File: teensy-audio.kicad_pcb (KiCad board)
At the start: 2 copper layers, 80 x 140 mm, 47 parts, among them J1 AudioJack2, J10 Conn_01x05, J11 Conn_01x02, J2 AudioJack2, J3 Barrel_Jack, J4 Conn_02x08_Odd_Even, J5 Conn_02x08_Odd_Even, J6 Conn_02x05_Odd_Even, J7 Conn_01x04, J8 Conn_01x04, J9 Conn_02x05_Odd_Even, SW1 RotaryEncoder_Switch, SW2/3 SW_Push, SW3/4 SW_Push, SW4/5 SW_Push, SW5/9 SW_Push, U1 LM358, U2 LM7805_TO220, U3 Teensy4.0

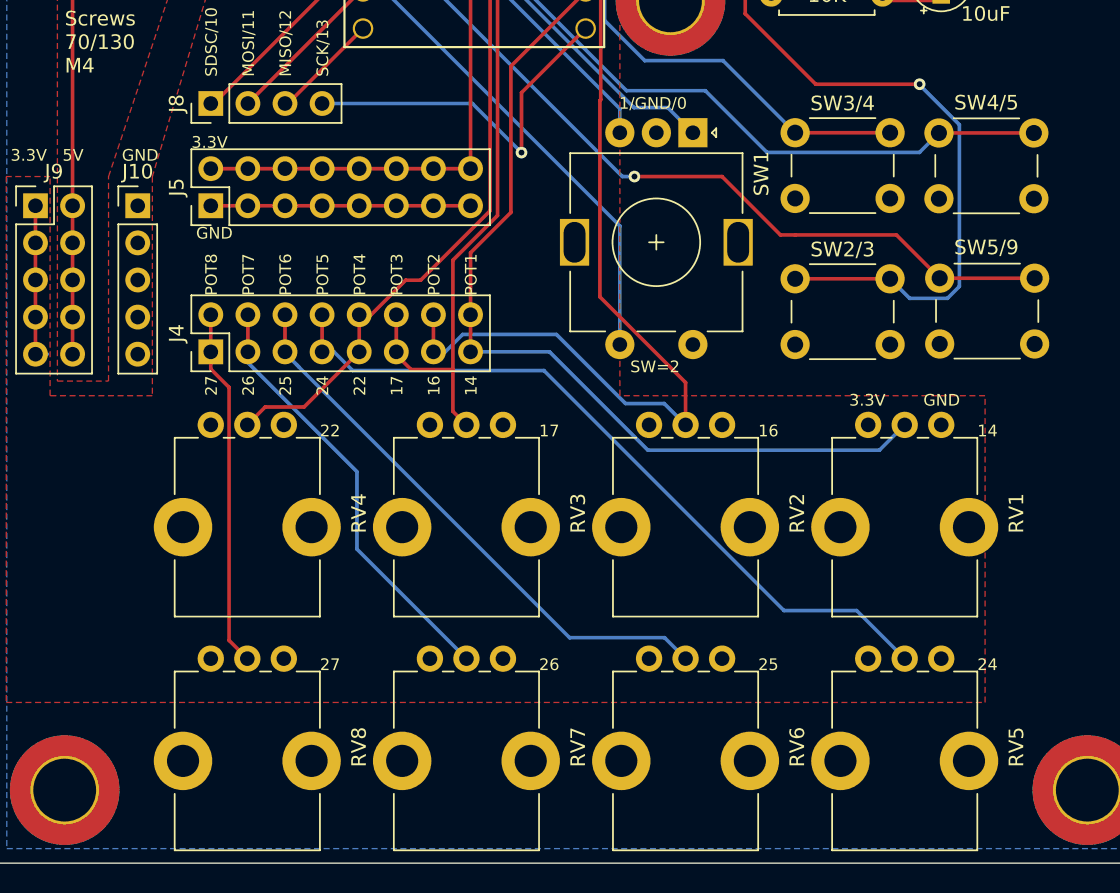
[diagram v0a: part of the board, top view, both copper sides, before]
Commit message: added oled screen
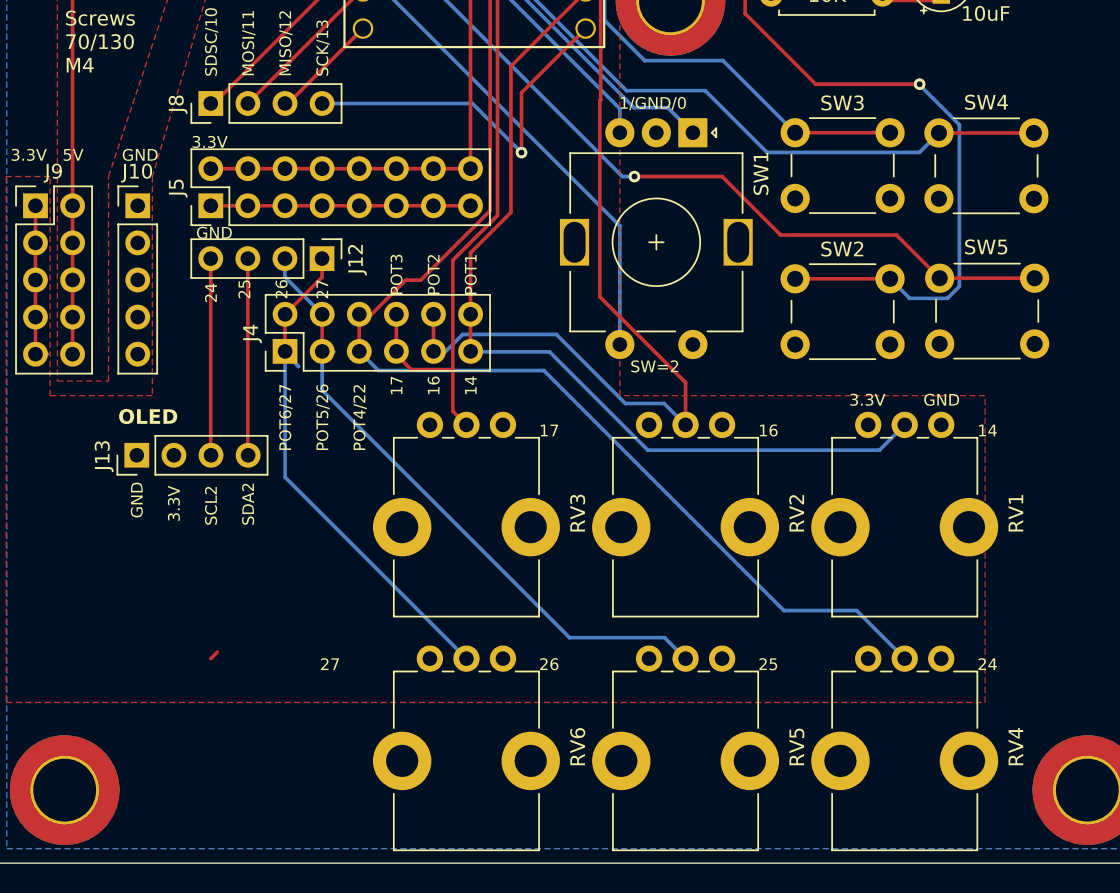
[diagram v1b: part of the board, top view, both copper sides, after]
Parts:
- removed RV7, RV8: 10K, Potentiometer_THT:Potentiometer_Bourns_PTV09A-1_Single_Vertical
- added J12: Conn_01x04, Connector_PinHeader_2.54mm:PinHeader_1x04_P2.54mm_Vertical, F.Cu at (182.6, 118.6)
- added J13: Conn_01x04, Connector_PinHeader_2.54mm:PinHeader_1x04_P2.54mm_Vertical, F.Cu at (169.9, 132.1)
- J4: value Conn_02x08_Odd_Even -> Conn_02x06_Odd_Even; footprint Connector_PinHeader_2.54mm:PinHeader_2x08_P2.54mm_Vertical -> Connector_PinHeader_2.54mm:PinHeader_2x06_P2.54mm_Vertical
- moved RV4 47.8 mm to (220.0, 146.0)
- moved RV5 15.0 mm to (205.0, 146.0)
- moved RV6 15.0 mm to (190.0, 146.0)
- moved J4 5.09 mm to (180.1, 125.0)
- renumbered SW2/3 to SW2, SW3/4 to SW3, SW4/5 to SW4, SW5/9 to SW5
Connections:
- J4 pad 1: POT8 -> POT6
- J4 pad 10: POT4 -> POT2
- J4 pad 11: POT3 -> POT1
- J4 pad 12: POT3 -> POT1
- J4 pad 2: POT8 -> POT6
- J4 pad 3: POT7 -> POT5
- J4 pad 4: POT7 -> POT5
- J4 pad 5: POT6 -> POT4
- J4 pad 6: POT6 -> POT4
- J4 pad 7: POT5 -> POT3
- J4 pad 8: POT5 -> POT3
- J4 pad 9: POT4 -> POT2
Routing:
- net POT4: track 62.2 -> 98.5 mm
- net POT7: track 29.7 -> 0.00 mm
- net POT8: track 24.6 -> 0.00 mm
- net SDA2: track 0.00 -> 13.5 mm
- net SCL2: track 0.00 -> 13.5 mm
- net POT5: track 51.1 -> 43.4 mm
- net POT6: track 38.7 -> 35.0 mm
- net +3.3V: track 74.5 -> 73.9 mm
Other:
- board text added: "OLED"
- board text added: "POT4/22"
- board text added: "POT5/26"
- board text added: "POT6/27"
- board text added: "SCL2"
- board text added: "SDA2"
- board text removed: "22"
- board text removed: "POT4"
- board text removed: "POT5"
- board text removed: "POT6"
- board text removed: "POT7"
- board text removed: "POT8"

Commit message: switch inputs and outputs positions on pcb
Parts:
- moved J1 22.4 mm to (210.1, 47.6)
- moved J2 22.4 mm to (187.7, 47.5)
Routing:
- net JACK_OUT: track 52.4 -> 74.8 mm
- net JACK_IN: track 42.6 -> 21.2 mm
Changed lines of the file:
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@@
   )
   (footprint "Connector_Audio:Jack_6.35mm_Neutrik_NMJ6HFD2-AU_Horizontal" (layer "F.Cu")
-    (at 210.071 47.575 90)
+    (at 187.706 47.498 90)
     (descr "M Series, 6.35mm (1/4in) stereo jack, switched, full threaded nose, straight PCB pins, gold plated contacts, https://www.neutrik.com/en/product/nmj6hfd2-au")
     (tags "neutrik jack m")
@@
   )
   (footprint "Connector_Audio:Jack_6.35mm_Neutrik_NMJ6HFD2-AU_Horizontal" (layer "F.Cu")
-    (at 187.706 47.498 90)
+    (at 210.071 47.575 90)
     (descr "M Series, 6.35mm (1/4in) stereo jack, switched, full threaded nose, straight PCB pins, gold plated contacts, https://www.neutrik.com/en/product/nmj6hfd2-au")
     (tags "neutrik jack m")
@@
     (effects (font (size 0.8 0.8) (thickness 0.08)) (justify left bottom))
   )
-  (gr_text "OUT" (at 215.646 57.15) (layer "F.SilkS")
+  (gr_text "OUT" (at 193.294 57.15) (layer "F.SilkS")
     (effects (font (size 1.5 1.5) (thickness 0.3) bold) (justify left bottom))
   )
@@
     (effects (font (size 0.8 0.8) (thickness 0.08)) (justify left bottom))
   )
-  (gr_text "IN" (at 194.056 57.658) (layer "F.SilkS")
+  (gr_text "IN" (at 216.662 57.15) (layer "F.SilkS")
     (effects (font (size 1.5 1.5) (thickness 0.3) bold) (justify left bottom))
   )
@@
   (segment (start 204 113) (end 203.17 113) (width 0.25) (layer "B.Cu") (net 35))
   (segment (start 207.01 86.36) (end 204.47 86.36) (width 1) (layer "B.Cu") (net 39))
-  (segment (start 216.916 56.134) (end 196.342 56.134) (width 1) (layer "F.Cu") (net 42))
-  (segment (start 196.342 56.134) (end 187.706 47.498) (width 1) (layer "F.Cu") (net 42))
   (segment (start 219.17 64.52) (end 219.17 59.44) (width 1) (layer "F.Cu") (net 42))
-  (segment (start 219.682 58.9) (end 216.916 56.134) (width 1) (layer "F.Cu") (net 42))
   (segment (start 219.17 59.44) (end 219.71 58.9) (width 0.25) (layer "F.Cu") (net 42))
   (segment (start 219.71 58.9) (end 219.682 58.9) (width 0.25) (layer "F.Cu") (net 42))
-  (segment (start 216.005 47.575) (end 227.33 58.9) (width 1) (layer "F.Cu") (net 43))
+  (segment (start 219.71 58.9) (end 219.71 57.214) (width 1) (layer "B.Cu") (net 42))
+  (segment (start 219.71 57.214) (end 210.071 47.575) (width 1) (layer "B.Cu") (net 42))
   (segment (start 227.65 88.04) (end 227.65 59.22) (width 1) (layer "F.Cu") (net 43))
-  (segment (start 210.071 47.575) (end 216.005 47.575) (width 1) (layer "F.Cu") (net 43))
   (segment (start 227.65 59.22) (end 227.33 58.9) (width 1) (layer "F.Cu") (net 43))
+  (segment (start 195.072 54.864) (end 187.706 47.498) (width 1) (layer "F.Cu") (net 43))
   (segment (start 226.79 88.9) (end 227.65 88.04) (width 1) (layer "F.Cu") (net 43))
+  (segment (start 227.33 58.9) (end 223.294 54.864) (width 1) (layer "F.Cu") (net 43))
+  (segment (start 223.294 54.864) (end 195.072 54.864) (width 1) (layer "F.Cu") (net 43))
   (segment (start 190.24 115) (end 187.7 115) (width 0.25) (layer "F.Cu") (net 44))
   (segment (start 180.08 115) (end 177.54 115) (width 0.25) (layer "F.Cu") (net 44))

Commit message: silkscreen cleanup
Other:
- board text added: "|<- 140mm ->| <- 130mm ->"
- board text added: "|<- 80mm ->| <- 70mm -> M4 holes"
- board text removed: "<- 140mm ->"
- board text removed: "<- 80mm ->"
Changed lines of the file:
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@@
     (property "ki_keywords" "audio jack receptacle mono phone headphone TS connector")
     (attr through_hole)
-    (fp_text reference "J2" (at 6.35 -3 90) (layer "F.SilkS")
+    (fp_text reference "J2" (at 20.574 0.254 90) (layer "F.SilkS")
         (effects (font (size 1 1) (thickness 0.15)))
     )
@@
     (property "ki_keywords" "audio jack receptacle mono phone headphone TS connector")
     (attr through_hole)
-    (fp_text reference "J1" (at 6.35 -3 90) (layer "F.SilkS")
+    (fp_text reference "J1" (at 20.651 0.749 90) (layer "F.SilkS")
         (effects (font (size 1 1) (thickness 0.15)))
     )
@@
     (effects (font (size 0.8 0.8) (thickness 0.08)) (justify left bottom))
   )
-  (gr_text "<- 140mm ->" (at 236 98 90) (layer "F.SilkS")
+  (gr_text "|<- 140mm ->|\n <- 130mm ->" (at 236 98 90) (layer "F.SilkS")
     (effects (font (size 1.5 1.5) (thickness 0.25) bold) (justify left bottom))
   )
@@
     (effects (font (size 0.8 0.8) (thickness 0.08)) (justify left bottom))
   )
-  (gr_text "<- 80mm ->" (at 165 100) (layer "F.SilkS")
+  (gr_text "|<- 80mm ->|\n <- 70mm ->\n  M4 holes" (at 162.814 99.314) (layer "F.SilkS")
     (effects (font (size 1.5 1.5) (thickness 0.25) bold) (justify left bottom))
   )
@@
   (zone (net 45) (net_name "+3.3V") (layer "F.Cu") (hatch edge 0.5)
     (priority 3)
-    (connect_pads (clearance 0.5))
+    (connect_pads (clearance 0.25))
     (min_thickness 0.25) (filled_areas_thickness no)
     (fill yes (thermal_gap 0.5) (thermal_bridge_width 0.5))

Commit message: split audio and digital grounds
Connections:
- C3 pad 2: GND -> GNDA
- J1 pad S: GND -> GNDA
- J2 pad S: GND -> GNDA
- J6 pad 2: LINE_IN_L_GND -> GNDA
- J6 pad 4: LINE_IN_R_GND -> GNDA
- J6 pad 7: LINE_OUT_GND -> GNDA
- J7 pad 2: GND -> GNDA
- J7 pad 3: GND -> GNDA
- R2 pad 2: GND -> GNDA
- R4 pad 2: GND -> GNDA
- R5 pad 2: GND -> GNDA
- U1 pad 4: GND -> GNDA
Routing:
- added copper zone on B.Cu, net GNDA

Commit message: decoupling capacitor for audio opamp
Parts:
- added C6: 10uF, Capacitor_THT:CP_Radial_D4.0mm_P2.00mm, F.Cu at (229.2, 75.4)
- added C7: 10nF, Capacitor_THT:CP_Radial_D4.0mm_P2.00mm, F.Cu at (229.2, 83.1)
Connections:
- J3 pad 3: (no net) -> VCC
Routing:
- net +5V: track 78.5 -> 10.6 mm
- net VCC: track 40.4 -> 2.69 mm
- net JACK_OUT: track 74.8 -> 81.5 mm
- net +3.3V: track 73.9 -> 73.2 mm
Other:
- board text added: "22"

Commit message: more space for oled display
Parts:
- moved J13 5.65 mm to (164.3, 132.8)
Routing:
- net SCL2: track 13.5 -> 16.5 mm
- net SDA2: track 13.5 -> 16.5 mm
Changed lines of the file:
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@@
   )
   (footprint "Connector_PinHeader_2.54mm:PinHeader_1x04_P2.54mm_Vertical" (layer "F.Cu")
-    (at 169.936 132.08 90)
+    (at 164.338 132.842 90)
     (descr "Through hole straight pin header, 1x04, 2.54mm pitch, single row")
     (tags "Through hole pin header THT 1x04 2.54mm single row")
@@
   (gr_rect (start 160 20) (end 240 160)
     (stroke (width 0.1) (type default)) (fill none) (layer "Edge.Cuts"))
-  (gr_text "GND" (at 170.434 136.398 90) (layer "F.SilkS")
+  (gr_text "GND" (at 164.846 137.16 90) (layer "F.SilkS")
     (effects (font (size 0.8 0.8) (thickness 0.08)) (justify left bottom))
   )
@@
     (effects (font (size 0.8 0.8) (thickness 0.08)) (justify left bottom))
   )
-  (gr_text "OLED" (at 168.656 130.048) (layer "F.SilkS")
+  (gr_text "OLED" (at 162.56 130.81) (layer "F.SilkS")
     (effects (font (size 1 1) (thickness 0.16) bold) (justify left bottom))
   )
@@
     (effects (font (size 0.8 0.8) (thickness 0.08)) (justify left bottom))
   )
-  (gr_text "SDA2" (at 178.054 136.906 90) (layer "F.SilkS")
+  (gr_text "SDA2" (at 172.466 137.668 90) (layer "F.SilkS")
     (effects (font (size 0.8 0.8) (thickness 0.08)) (justify left bottom))
   )
@@
     (effects (font (size 0.8 0.8) (thickness 0.08)) (justify left bottom))
   )
-  (gr_text "3.3V" (at 172.974 136.652 90) (layer "F.SilkS")
+  (gr_text "3.3V" (at 167.386 137.414 90) (layer "F.SilkS")
     (effects (font (size 0.8 0.8) (thickness 0.08)) (justify left bottom))
   )
@@
     (effects (font (size 0.8 0.8) (thickness 0.08)) (justify left bottom))
   )
-  (gr_text "SCL2" (at 175.514 136.906 90) (layer "F.SilkS")
+  (gr_text "SCL2" (at 169.926 137.668 90) (layer "F.SilkS")
     (effects (font (size 0.8 0.8) (thickness 0.08)) (justify left bottom))
   )
@@
   (segment (start 163 125.16) (end 163.8111 125.16) (width 0.25) (layer "B.Cu") (net 42))
   (segment (start 205 130) (end 205.384 130) (width 0.25) (layer "B.Cu") (net 42))
-  (segment (start 177.536 118.618) (end 177.536 132.06) (width 0.25) (layer "F.Cu") (net 43))
-  (segment (start 177.536 132.06) (end 177.556 132.08) (width 0.25) (layer "F.Cu") (net 43))
-  (segment (start 174.996 118.618) (end 174.996 132.06) (width 0.25) (layer "F.Cu") (net 44))
-  (segment (start 174.996 132.06) (end 175.016 132.08) (width 0.25) (layer "F.Cu") (net 44))
+  (segment (start 177.536 127.264) (end 171.958 132.842) (width 0.25) (layer "F.Cu") (net 43))
+  (segment (start 177.536 118.618) (end 177.536 127.264) (width 0.25) (layer "F.Cu") (net 43))
+  (segment (start 174.996 127.264) (end 169.418 132.842) (width 0.25) (layer "F.Cu") (net 44))
+  (segment (start 174.996 118.618) (end 174.996 127.264) (width 0.25) (layer "F.Cu") (net 44))
   (zone (net 5) (net_name "+5V") (layer "F.Cu") (hatch edge 0.5)
     (priority 2)

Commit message: corrected barrel plug
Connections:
- J3 pad 1: GND -> VCC
- J3 pad 2: VCC -> GND
- J3 pad 3: VCC -> GND
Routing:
- net VCC: track 2.69 -> 0.62 mm
- net GND: track 17.8 -> 19.8 mm
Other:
- board text added: "9V . = + o = -"
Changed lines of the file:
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@@
       (stroke (width 0.1) (type solid)) (layer "F.Fab"))
     (pad "1" thru_hole rect (at 0 0 180) (size 4.6 2) (drill oval 3.6 1) (layers "*.Cu" "*.Mask")
-      (net 41 "GND") (pintype "power_out"))
+      (net 4 "VCC") (pintype "power_out"))
     (pad "2" thru_hole oval (at 0 6.3 180) (size 4.2 2) (drill oval 3.2 1) (layers "*.Cu" "*.Mask")
-      (net 4 "VCC") (pintype "passive"))
+      (net 41 "GND") (pintype "passive"))
     (pad "3" thru_hole oval (at 4.8 2.9 180) (size 2 4.2) (drill oval 1 3.2) (layers "*.Cu" "*.Mask")
-      (net 4 "VCC"))
+      (net 41 "GND"))
     (model "${KICAD6_3DMODEL_DIR}/Connector_BarrelJack.3dshapes/BarrelJack_GCT_DCJ200-10-A_Horizontal.wrl"
       (offset (xyz 0 0 0))
@@
     (effects (font (size 0.8 0.8) (thickness 0.08)) (justify left bottom))
   )
+  (gr_text "9V\n. = +\no = -" (at 166.116 34.036) (layer "F.SilkS")
+    (effects (font (size 1 1) (thickness 0.2) bold) (justify left bottom))
+  )
   (gr_text "MISO/12" (at 180.594 106.172 90) (layer "F.SilkS")
     (effects (font (size 0.8 0.8) (thickness 0.08)) (justify left bottom))
@@
   (segment (start 223.51 83.04) (end 223.51 87.62) (width 1) (layer "F.Cu") (net 2))
   (segment (start 220.98 100.57) (end 225 100.57) (width 1) (layer "F.Cu") (net 3))
-  (segment (start 177.942 29.006) (end 178.612 29.006) (width 0.25) (layer "F.Cu") (net 4))
   (segment (start 178.035 50.22) (end 178.65 50.22) (width 0.25) (layer "F.Cu") (net 4))
-  (segment (start 177.942 29.006) (end 176.542 29.006) (width 0.25) (layer "F.Cu") (net 4))
   (segment (start 170.72 57.84) (end 170.72 57.3765) (width 0.25) (layer "F.Cu") (net 5))
   (segment (start 165.54 120.08) (end 165.54 117.54) (width 0.25) (layer "F.Cu") (net 5))
@@
   (segment (start 182.62 115) (end 180.08 115) (width 0.25) (layer "F.Cu") (net 41))
   (segment (start 177.54 115) (end 175 115) (width 0.25) (layer "F.Cu") (net 41))
+  (segment (start 177.942 29.006) (end 178.612 29.006) (width 0.25) (layer "F.Cu") (net 41))
   (segment (start 192.78 115) (end 190.24 115) (width 0.25) (layer "F.Cu") (net 41))
   (segment (start 185.16 115) (end 182.62 115) (width 0.25) (layer "F.Cu") (net 41))
+  (segment (start 177.942 29.006) (end 176.542 29.006) (width 0.25) (layer "F.Cu") (net 41))
   (segment (start 187.7 115) (end 185.16 115) (width 0.25) (layer "F.Cu") (net 41))
   (segment (start 220.478 145.522) (end 220 146) (width 0.25) (layer "F.Cu") (net 42))
